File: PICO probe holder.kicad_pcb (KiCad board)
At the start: 2 copper layers, 43.2 x 94 mm, 5 parts, among them J1 Conn_01x07_Male, J2 Conn_02x02_Odd_Even, SW1 SW_Push, U1 Pico

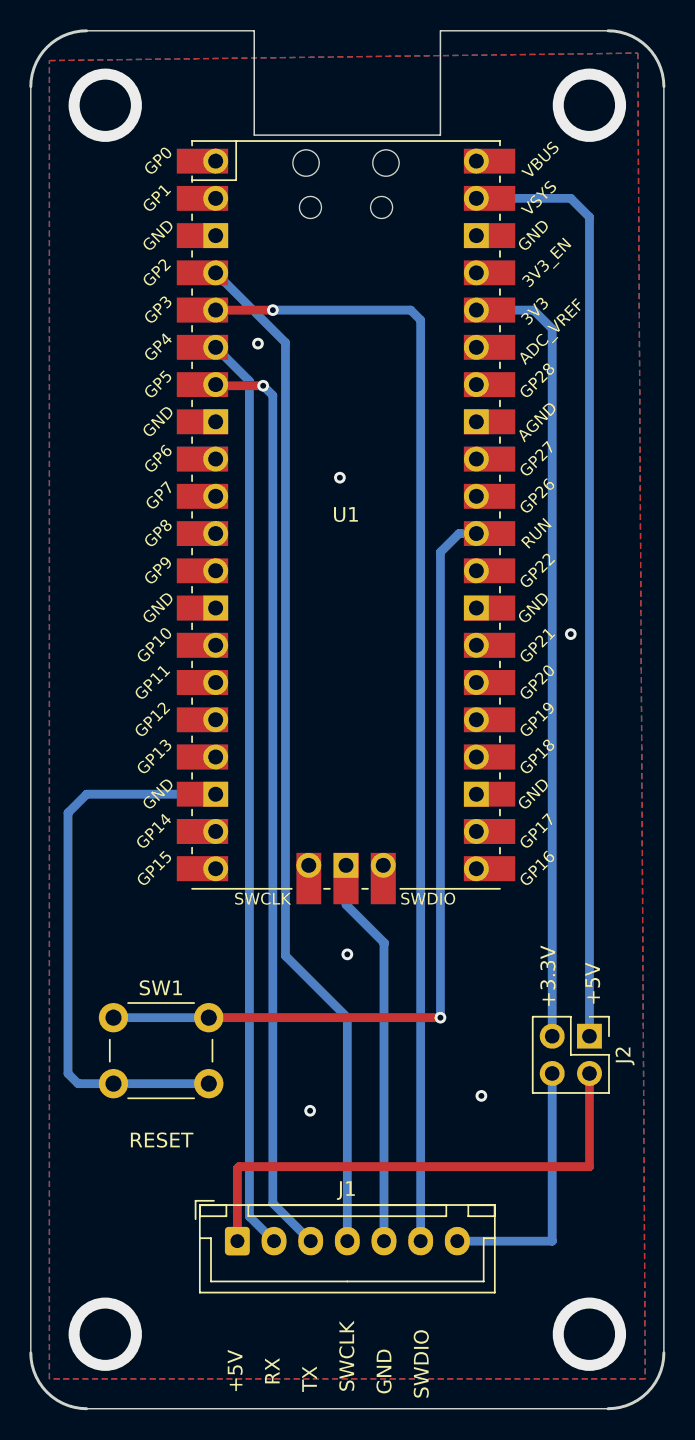
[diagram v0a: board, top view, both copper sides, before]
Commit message: optimized ground Layer, case design added V1.1
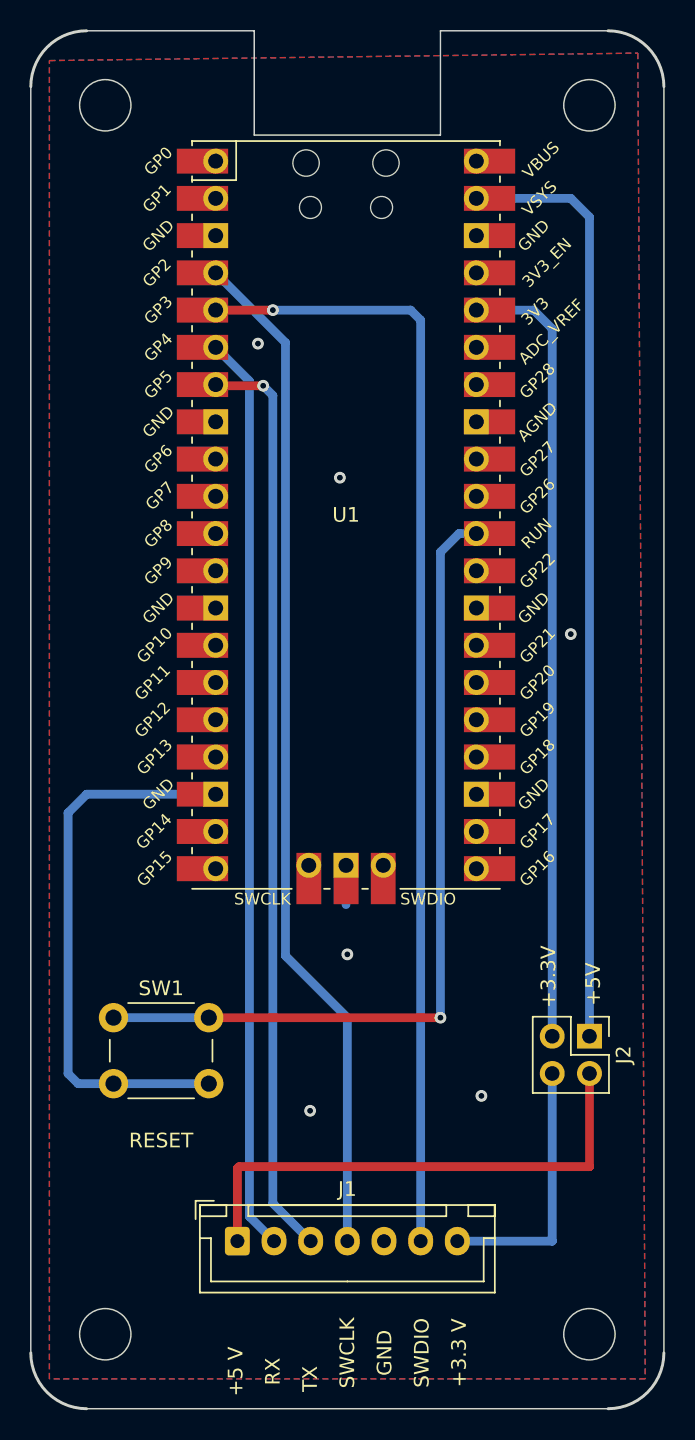
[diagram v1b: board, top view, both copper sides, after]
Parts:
- removed REF**: ESD-Logo_6.6x6mm_SilkScreen, Symbol:ESD-Logo_6.6x6mm_SilkScreen
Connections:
- J1 pad 5: Net-(J1-Pad5) -> GND
- U1 pad 13: unconnected-(U1-Pad13) -> GND
- U1 pad 23: unconnected-(U1-Pad23) -> GND
- U1 pad 28: unconnected-(U1-Pad28) -> GND
- U1 pad 3: unconnected-(U1-Pad3) -> GND
- U1 pad 33: unconnected-(U1-Pad33) -> GND
- U1 pad 38: unconnected-(U1-Pad38) -> GND
- U1 pad 42: Net-(J1-Pad5) -> GND
- U1 pad 8: unconnected-(U1-Pad8) -> GND
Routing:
- net Net-(J1-Pad5): track 26.7 -> 0.00 mm
- net GND: track 38.3 -> 40.9 mm, vias 10 -> 6
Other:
- outline, holes or cut-outs redrawn
- board text added: "+3.3 V"
- board text added: "+5 V"
- board text added: "PICO probeholder Board v1.1.0 License CC BY-NC-SA 4.0 https://github.com/ene9ba/PicoProbeHolder"
- board text removed: "PICO probeholder Board v1.0.0 License CC BY-NC-SA 4.0 https://github.com/ene9ba/PicoProbeHolder"
